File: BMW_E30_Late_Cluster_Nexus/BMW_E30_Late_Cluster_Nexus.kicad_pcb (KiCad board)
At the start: 2 copper layers, 356.8 x 150 mm, 19 parts, among them J1 Blue, J2 White, J3 Yellow

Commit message: All Footprints Added to Nexus
All footprints have been added to the nexus board project. Next step is to import them to the layout.
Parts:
- moved J1 1.00 mm to (337.1, 162.8)
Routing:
- net Brake lining: track 594.6 -> 0.00 mm
- net 12V: track 522.6 -> 0.00 mm
- net GND: track 411.4 -> 0.00 mm
- net GND lighting: track 365.4 -> 0.00 mm
- net Park brake: track 240.4 -> 0.00 mm
- net Turn L: track 176.8 -> 0.00 mm
- net High beam: track 157.1 -> 0.00 mm
- net Turn R: track 156.1 -> 0.00 mm
- net Check: track 135.2 -> 0.00 mm
- net Brake fluid: track 115.9 -> 0.00 mm
- net Fog front: track 95.5 -> 0.00 mm
- net Fog rear: track 57.6 -> 0.00 mm
- net Oil pressure: track 57.0 -> 0.00 mm
- net Temp warn: track 50.0 -> 0.00 mm
- net Fuel warn: track 33.9 -> 0.00 mm

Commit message: Nexus Layout Updates
Layout is about 50% complete. Need to verify exact component locations with early model board.
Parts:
- added D6: 1N4004, Diode_THT:D_DO-41_SOD81_P12.70mm_Horizontal, B.Cu at (332.1, 228.0)
- added D64: 1N4004, Diode_THT:D_DO-41_SOD81_P10.16mm_Horizontal, B.Cu at (220.1, 126.9)
- added D7: 1N4004, Diode_THT:D_DO-41_SOD81_P12.70mm_Horizontal, B.Cu at (53.6, 154.8)
- added D8: 1N4004, Diode_THT:D_DO-41_SOD81_P12.70mm_Horizontal, B.Cu at (303.6, 162.8)
- added J4: Speedometer, BMW_Cluster_Connectors:ConnectorIV_Late, F.Cu at (213.9, 130.7)
- added J5: SI Connector, BMW_Cluster_Connectors:ConnectorV_Late, F.Cu at (240.1, 221.2)
- added J6: Tachometer, BMW_Cluster_Connectors:Tach_EG_Socket_Late, F.Cu at (227.1, 150.5)
- added Q1: BC327, Package_TO_SOT_THT:TO-92_Inline_Wide, B.Cu at (60.6, 148.0)
- added R10: 10k, Resistor_THT:R_Axial_DIN0207_L6.3mm_D2.5mm_P10.16mm_Horizontal, B.Cu at (314.1, 172.5)
- added R100: ??, Resistor_THT:R_Axial_DIN0207_L6.3mm_D2.5mm_P15.24mm_Horizontal, B.Cu at (61.1, 153.8)
- added R101: ??, Resistor_THT:R_Axial_DIN0207_L6.3mm_D2.5mm_P15.24mm_Horizontal, B.Cu at (57.6, 153.8)
- added R11: 4k7, Resistor_THT:R_Axial_DIN0207_L6.3mm_D2.5mm_P15.24mm_Horizontal, B.Cu at (67.6, 168.2)
- added R12: 390R 0W5, Resistor_THT:R_Axial_DIN0309_L9.0mm_D3.2mm_P15.24mm_Horizontal, B.Cu at (68.6, 149.5)
- added R2: 150R, Resistor_THT:R_Axial_DIN0414_L11.9mm_D4.5mm_P20.32mm_Horizontal, B.Cu at (338.6, 186.7)
- added R3: 68R 1W, Resistor_THT:R_Axial_DIN0414_L11.9mm_D4.5mm_P20.32mm_Horizontal, B.Cu at (53.6, 176.2)
- added R5: 220R 1W, Resistor_THT:R_Axial_DIN0414_L11.9mm_D4.5mm_P20.32mm_Horizontal, B.Cu at (377.8, 162.0)
- added R9: 10R, Resistor_THT:R_Axial_DIN0207_L6.3mm_D2.5mm_P15.24mm_Horizontal, B.Cu at (300.6, 190.8)
- added U1: Coolant Temp, BMW_Cluster_Connectors:Gauge_Temp, F.Cu at (354.3, 186.5)
- added U2: Fuel Gauge, BMW_Cluster_Connectors:Gauge_Fuel, F.Cu at (62.9, 186.5)
- J1: footprint TE_AMP:TE_827881-3 -> BMW_Cluster_Connectors:TE_827881-3
- J2: footprint TE_AMP:TE_827881-2 -> BMW_Cluster_Connectors:TE_827881-2
- J3: footprint TE_AMP:TE_827881-1 -> BMW_Cluster_Connectors:TE_827881-1
- LA1, LA2: footprint mount:2821MF -> BMW_Cluster_Connectors:2821MF
- LA10: value Brake lining -> Brake pad; footprint mount:2721MF -> BMW_Cluster_Connectors:2721MF
- LA11, LA12, LA15, LA16, LA3, LA4, LA5, LA6, LA9: footprint mount:2721MF -> BMW_Cluster_Connectors:2721MF
- LA13: value Oil pressure -> Oil Pressure; footprint mount:2721MF -> BMW_Cluster_Connectors:2721MF
- LA14: value Fuel reserve -> Fuel Reserve; footprint mount:2721MF -> BMW_Cluster_Connectors:2721MF
- LA7: value Fog rear -> Fog Rear; footprint mount:2721MF -> BMW_Cluster_Connectors:2721MF
- LA8: value Fog front -> Fog Front; footprint mount:2721MF -> BMW_Cluster_Connectors:2721MF
- moved LA7 19.9 mm to (147.5, 212.2), turned to 0 degrees
- moved LA8 19.9 mm to (127.6, 212.2), turned to 90 degrees
- turned LA1 to 0 degrees
- turned LA2 to -40 degrees
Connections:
- net 5V renamed S-DKV
- net Fog front renamed Fog_ind+
- net High beam renamed High_beam_ind
- net R renamed +12_T15_ACC
- net Turn L renamed LH_ind
- net Turn R renamed RH_ind
- J1 pad 1: 12V -> +12_Start_T50
- J1 pad 10: unconnected-(J1-Pin_10-Pad10) -> +12_T15
- J1 pad 11: unconnected-(J1-Pin_11-Pad11) -> Fuel_rate_input
- J1 pad 14: Battery 1 -> Charge_ind+
- J1 pad 16: Battery 2 -> Charge_ind-
- J1 pad 17: Brake fluid -> Brake_fluid_ind-
- J1 pad 18: Oil pressure -> OIl_pressure_ind-
- J1 pad 19: unconnected-(J1-Pin_19-Pad19) -> +12_T15
- J1 pad 2: 12V -> +12_T30
- J1 pad 20: GND -> GNDPWR
- J1 pad 21: Brake lining -> Brake_wear_sig_1
- J1 pad 22: SI reset -> SI_RST
- J1 pad 23: 12V -> +12_T15
- J1 pad 25: Temp warn -> Overheat_ind-
- J1 pad 26: Temp gauge -> Eng_temp_sensor
- J1 pad 3: unconnected-(J1-Pin_3-Pad3) -> Charge_ind-
- J1 pad 6: unconnected-(J1-Pin_6-Pad6) -> +12_T15
- J1 pad 7: 12V -> Raw_RPM_input
- J1 pad 8: unconnected-(J1-Pin_8-Pad8) -> Reverse_gear
- J1 pad 9: unconnected-(J1-Pin_9-Pad9) -> 5th_gear
- J2 pad 1: Park brake -> Park_brake_ind-
- J2 pad 10: unconnected-(J2-Pin_10-Pad10) -> Wheel_spd_output
- J2 pad 12: unconnected-(J2-Pin_12-Pad12) -> Wheel_spd_input
- J2 pad 14: Fog rear -> Rear_fog_ind+
- J2 pad 15: unconnected-(J2-Pin_15-Pad15) -> DKV-DEFEKT
- J2 pad 16: GND -> GNDPWR
- J2 pad 19: unconnected-(J2-Pin_19-Pad19) -> KL_31h
- J2 pad 2: unconnected-(J2-Pin_2-Pad2) -> N-DKV
- J2 pad 21: GND -> GNDPWR
- J2 pad 23: 12V -> Illum+
- J2 pad 24: GND lighting -> Illum-
- J2 pad 26: Brake lining -> Brake_wear_sig_2
- J2 pad 3: GND -> GNDPWR
- J2 pad 4: Fuel gauge -> Fuel_level
- J2 pad 5: Fuel warn -> Low_Fuel_ind-
- J2 pad 6: 12V -> +12_T15
- J2 pad 8: GND -> GNDPWR
- J2 pad 9: unconnected-(J2-Pin_9-Pad9) -> K-DKV
- J3 pad 1: GND -> GNDPWR
- J3 pad 10: 12V -> +12_T30
- J3 pad 11: 12V -> Engine_spd_input
- J3 pad 12: unconnected-(J3-Pin_12-Pad12) -> Fuel_rate_input
- J3 pad 14: 12V -> +12_T15
- J3 pad 15: 12V -> +12_T15
- J3 pad 16: unconnected-(J3-Pin_16-Pad16) -> GNDPWR
- J3 pad 17: unconnected-(J3-Pin_17-Pad17) -> Low_Fuel_ind-
- J3 pad 18: unconnected-(J3-Pin_18-Pad18) -> Fuel_level
- J3 pad 19: Park brake -> GNDPWR
- J3 pad 2: 12V -> +12_T15
- J3 pad 20: 12V -> Illum+
- J3 pad 21: GND lighting -> Illum-
- J3 pad 22: 12V -> +12_Start_T50
- J3 pad 23: 12V -> +12_T30
- J3 pad 24: 12V -> Engine_spd_input
- J3 pad 25: unconnected-(J3-Pin_25-Pad25) -> Fuel_rate_input
- J3 pad 26: Analog speed -> Wheel_spd_output
- J3 pad 3: unconnected-(J3-Pin_3-Pad3) -> GNDPWR
- J3 pad 4: Fuel warn -> Low_Fuel_ind-
- J3 pad 5: Fuel gauge -> Fuel_level
- J3 pad 6: Park brake -> GNDPWR
- J3 pad 7: 12V -> Illum+
- J3 pad 8: GND lighting -> Illum-
- J3 pad 9: 12V -> +12_Start_T50
- LA1 pad 1: 12V -> Illum-
- LA1 pad 2: GND lighting -> Illum+
- LA10 pad 1: 12V -> GNDPWR
- LA10 pad 2: Brake lining -> Net-(LA10-+)
- LA11 pad 1: 12V -> Brake_fluid_ind-
- LA11 pad 2: Brake fluid -> +12_T15
- LA12 pad 1: unconnected-(LA12---Pad1) -> Charge_ind+
- LA12 pad 2: unconnected-(LA12-+-Pad2) -> Charge_ind-
- LA13 pad 1: 12V -> OIl_pressure_ind-
- LA13 pad 2: Oil pressure -> +12_T15
- LA14 pad 1: 12V -> +12_T15
- LA14 pad 2: Fuel warn -> Low_Fuel_ind-
- LA15 pad 1: Temp warn -> +12_T15
- LA15 pad 2: 12V -> Overheat_ind-
- LA2 pad 1: 12V -> Illum+
- LA2 pad 2: GND lighting -> Illum-
- LA3 pad 1: GND -> +12_T15
- LA4 pad 2: GND -> GNDPWR
- LA5 pad 2: GND -> GNDPWR
- LA6 pad 1: GND -> GNDPWR
- LA7 pad 1: Fog rear -> GNDPWR
- LA7 pad 2: GND -> Rear_fog_ind+
- LA8 pad 2: GND -> GNDPWR
- LA9 pad 1: 12V -> +12_T15
- LA9 pad 2: Park brake -> Park_brake_ind-
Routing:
- net GNDPWR: track 0.00 -> 764.2 mm, vias 0 -> 2
- net +12_T15: track 0.00 -> 497.3 mm, vias 0 -> 2
- net Illum+: track 0.00 -> 457.5 mm, vias 0 -> 2
- net Illum-: track 0.00 -> 420.2 mm, vias 0 -> 2
- net Wheel_spd_output: track 0.00 -> 369.4 mm
- net Park_brake_ind-: track 0.00 -> 364.9 mm, vias 0 -> 4
- net +12_T15_ACC: track 0.00 -> 359.9 mm, vias 0 -> 2
- net Low_Fuel_ind-: track 0.00 -> 298.7 mm
- net Fuel_level: track 0.00 -> 281.2 mm
- net Wheel_spd_input: track 0.00 -> 259.2 mm
- net Net-(D8-K): track 0.00 -> 238.2 mm, vias 0 -> 2
- net LH_ind: track 0.00 -> 232.8 mm
- net +12_T30: track 0.00 -> 220.5 mm, vias 0 -> 2
- net Fuel_rate_input: track 0.00 -> 200.0 mm
- net Check: track 0.00 -> 168.6 mm, vias 0 -> 2
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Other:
- outline, holes or cut-outs redrawn
- board text added: "BMW PN: 1 377 374 or 1 381 952"
- board text added: "E30"
- board text added: "Glow Plug [Diesel]"
- board text added: "Nexus board replacement"
- board text added: "Revision: 1"
- board text removed: "1 377 374"
- board text removed: "E 30"
- board text removed: "Glow plug [Diesel]"
- board text removed: "Main board replacement"
- board text removed: "Polytechnic"
- board text removed: "Systems"

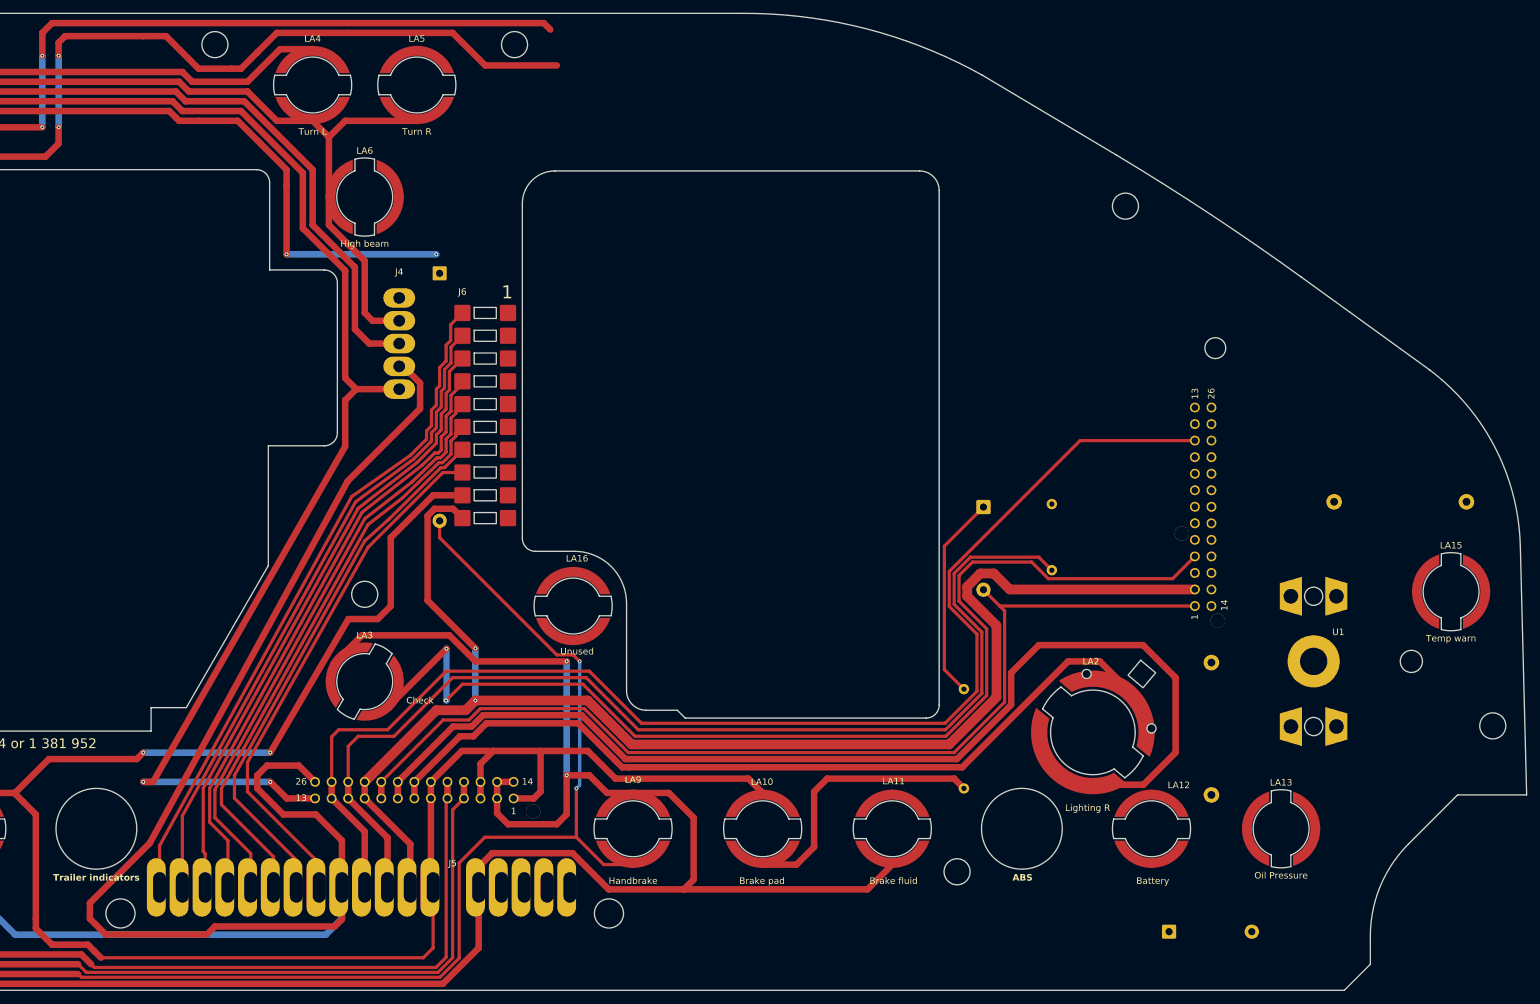
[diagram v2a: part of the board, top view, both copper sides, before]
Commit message: Nexus Trace Layout Completed
Trace layout is complete. Still need to verify some component locations
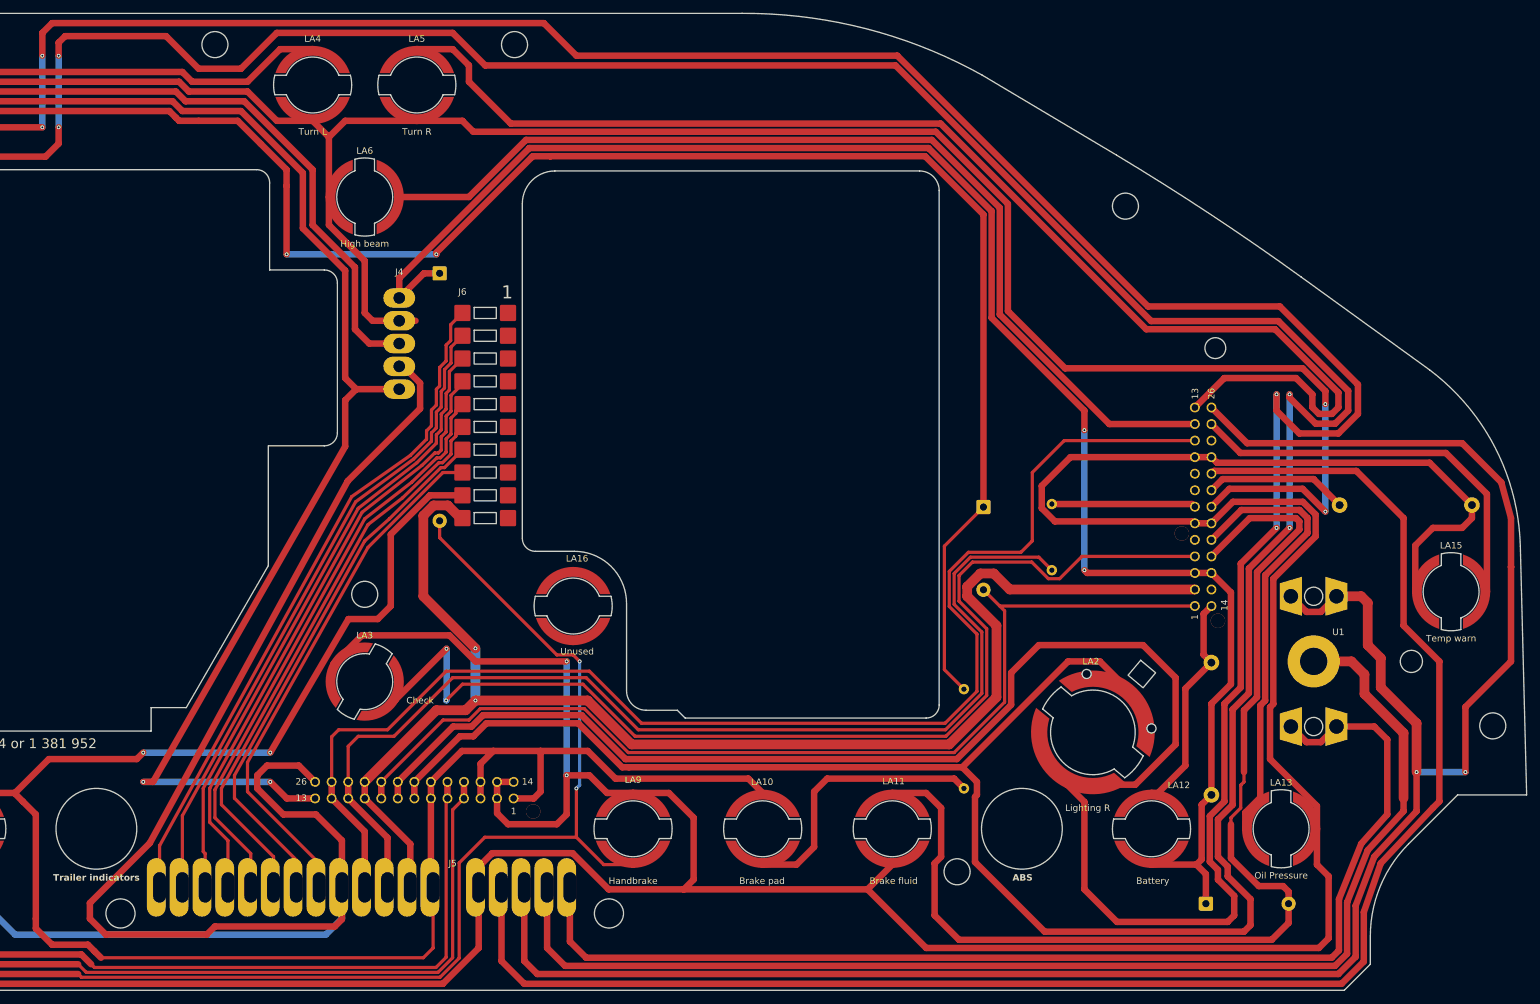
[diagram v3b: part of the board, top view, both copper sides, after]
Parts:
- moved D6 7.10 mm to (337.8, 223.7)
- moved R5 0.98 mm to (378.6, 162.5)
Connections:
- LA14 pad 1: +12_T15 -> unconnected-(LA14---Pad1)
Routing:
- net Eng_temp_sensor: track 0.00 -> 320.0 mm, vias 0 -> 2
- net Illum+: track 457.5 -> 765.6 mm, vias 2 -> 4
- net Illum-: track 420.2 -> 718.8 mm, vias 2 -> 4
- net +12_T15: track 497.3 -> 783.2 mm
- net Charge_ind-: track 0.00 -> 256.5 mm, vias 0 -> 2
- net SI_RST: track 0.00 -> 253.6 mm
- net GNDPWR: track 764.2 -> 971.9 mm, vias 2 -> 4
- net RH_ind: track 0.00 -> 194.9 mm
- net Temp_GND: track 0.00 -> 190.8 mm
- net Temp_+Ub: track 0.00 -> 180.1 mm
- net Brake_fluid_ind-: track 0.00 -> 170.3 mm
- net High_beam_ind: track 0.00 -> 153.3 mm
- net Net-(D8-K): track 238.2 -> 377.2 mm
- net OIl_pressure_ind-: track 0.00 -> 68.8 mm
- net Overheat_ind-: track 0.00 -> 61.7 mm
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
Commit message: Rotate Right Illum Bulb
Changed orientation of the right side illumination bulb
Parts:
- turned LA2 to -30 degrees
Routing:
- net Illum-: track 718.8 -> 715.9 mm
- net Illum+: track 765.6 -> 764.0 mm

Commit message: Standardized Board Location In Editor
Made the board location the same in both projects so component locations can be corrected from sample runs of the early boards.
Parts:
- moved D6 0.60 mm to (337.1, 223.7)
- moved D8 0.60 mm to (303.0, 162.8)
- moved J1 0.60 mm to (336.5, 162.8)
- moved LA11 0.60 mm to (289.0, 212.2)
- moved LA13 0.60 mm to (348.7, 212.2)
- moved LA9 0.60 mm to (249.2, 212.2)
- moved R10 0.60 mm to (313.5, 172.5)
- moved R2 0.60 mm to (338.0, 186.7)
- moved R5 0.60 mm to (378.0, 162.5)
- moved R9 0.60 mm to (300.0, 190.8)
- moved U1 0.60 mm to (353.7, 186.5)
- moved D7 0.60 mm to (53.0, 154.8)
- moved LA14 0.60 mm to (42.8, 174.4)
- moved Q1 0.60 mm to (60.0, 148.0)
- moved R100 0.60 mm to (60.5, 153.8)
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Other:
- outline, holes or cut-outs redrawn

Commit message: Layout Updates to Match Early
Changed a few light bulb component locations to match the correct locations on the early model boards.
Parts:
- moved LA15 0.81 mm to (374.6, 175.0)
- moved LA14 0.45 mm to (43.0, 174.0)
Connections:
- LA14 pad 1: unconnected-(LA14---Pad1) -> +12_T15
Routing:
- net Wheel_spd_output: track 369.4 -> 370.6 mm
- net +12_T15: track 783.2 -> 782.3 mm
- net Overheat_ind-: track 61.7 -> 60.9 mm
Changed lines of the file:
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@@
 	(net 60 "Net-(U2-Vcc)")
 	(net 61 "Net-(LA10-+)")
-	(net 62 "unconnected-(LA14---Pad1)")
 	(footprint "BMW_Cluster_Connectors:2721MF"
 		(layer "F.Cu")
@@
 	(footprint "BMW_Cluster_Connectors:2721MF"
 		(layer "F.Cu")
-		(at 374.8 175.8 90)
+		(at 374.65 175 90)
 		(property "Reference" "LA15"
 			(at 7.099836 0.003178 0)
@@
 	(footprint "BMW_Cluster_Connectors:2721MF"
 		(layer "F.Cu")
-		(at 42.8 174.4 90)
+		(at 43 174 90)
 		(property "Reference" "LA14"
 			(at 7.099836 0.003178 0)
@@
 			(size 1 1)
 			(layers "F.Cu" "F.Mask")
-			(net 62 "unconnected-(LA14---Pad1)")
+			(net 13 "+12_T15")
 			(pinfunction "-")
 			(pintype "passive")
@@
 	)
 	(segment
-		(start 378 164.5)
-		(end 376.5 166)
+		(start 372 166)
+		(end 369.15 168.85)
 		(width 1)
 		(layer "F.Cu")
@@
 	)
 	(segment
-		(start 51.5 216.5)
-		(end 54.5 224)
-		(width 1)
-		(layer "F.Cu")
-		(net 13)
-	)
-	(segment
 		(start 221 182.5)
 		(end 207.58686 182.5)
@@
 	)
 	(segment
-		(start 372 166)
-		(end 369.3 168.7)
+		(start 225.5 221.2)
+		(end 225.5 230.5)
 		(width 1)
 		(layer "F.Cu")
@@
 	)
 	(segment
+		(start 225.5 230.5)
+		(end 220.001 235.999)
+		(width 1)
+		(layer "F.Cu")
+		(net 13)
+	)
+	(segment
+		(start 37.5 174)
+		(end 37.5 169.5)
+		(width 1)
+		(layer "F.Cu")
+		(net 13)
+	)
+	(segment
 		(start 41 166)
 		(end 51.5 166)
@@
 	)
 	(segment
-		(start 76.33 165.3)
-		(end 79.46 165.3)
+		(start 54.5 224)
+		(end 51.5 216.5)
 		(width 1)
 		(layer "F.Cu")
@@
 	)
 	(segment
-		(start 37.3 169.7)
-		(end 41 166)
+		(start 76.33 165.3)
+		(end 79.46 165.3)
 		(width 1)
 		(layer "F.Cu")
@@
 	)
 	(segment
-		(start 369.3 168.7)
-		(end 369.3 175.8)
+		(start 258.5 220)
+		(end 257 221.5)
 		(width 1)
 		(layer "F.Cu")
@@
 	)
 	(segment
-		(start 258.5 220)
-		(end 257 221.5)
+		(start 55 232.5)
+		(end 54.5 224)
 		(width 1)
 		(layer "F.Cu")
@@
 	)
 	(segment
-		(start 228.32 209.82)
-		(end 228.32 207.54)
+		(start 378 162.5)
+		(end 378 164.5)
 		(width 1)
 		(layer "F.Cu")
@@
 	)
 	(segment
-		(start 347 201.5)
-		(end 347 193.538362)
+		(start 228.32 209.82)
+		(end 228.32 207.54)
 		(width 1)
 		(layer "F.Cu")
@@
 	)
 	(segment
-		(start 376.5 166)
-		(end 372 166)
+		(start 347 201.5)
+		(end 347 193.538362)
 		(width 1)
 		(layer "F.Cu")
@@
 	)
 	(segment
-		(start 220.001 235.999)
-		(end 225.5 230.5)
+		(start 53 167.5)
+		(end 55.5 167.5)
 		(width 1)
 		(layer "F.Cu")
@@
 	)
 	(segment
-		(start 53 167.5)
-		(end 55.5 167.5)
+		(start 294.2 230.5)
+		(end 354.5 230.5)
 		(width 1)
 		(layer "F.Cu")
@@
 	)
 	(segment
-		(start 294.2 230.5)
-		(end 354.5 230.5)
+		(start 369.15 168.85)
+		(end 369.15 175)
 		(width 1)
 		(layer "F.Cu")
@@
 	)
 	(segment
+		(start 37.5 169.5)
+		(end 41 166)
+		(width 1)
+		(layer "F.Cu")
+		(net 13)
+	)
+	(segment
 		(start 378 162.5)
 		(end 371.5 156)
@@
 	)
 	(segment
-		(start 354.2 217.7)
-		(end 354.2 212.2)
+		(start 376.5 166)
+		(end 372 166)
 		(width 1)
 		(layer "F.Cu")
@@
 	)
 	(segment
-		(start 38 203)
-		(end 51.5 216.5)
+		(start 354.2 217.7)
+		(end 354.2 212.2)
 		(width 1)
 		(layer "F.Cu")
@@
 	)
 	(segment
+		(start 220.001 235.999)
+		(end 58.499 235.999)
+		(width 1)
+		(layer "F.Cu")
+		(net 13)
+	)
+	(segment
 		(start 354.2 208.7)
 		(end 347 201.5)
@@
 	)
 	(segment
+		(start 58.499 235.999)
+		(end 55 232.5)
+		(width 1)
+		(layer "F.Cu")
+		(net 13)
+	)
+	(segment
+		(start 51.5 216.5)
+		(end 38 203)
+		(width 1)
+		(layer "F.Cu")
+		(net 13)
+	)
+	(segment
 		(start 352.036362 161.998)
 		(end 341.302 161.998)
@@
 	)
 	(segment
-		(start 38 195.355945)
-		(end 38 203)
+		(start 38 203)
+		(end 38 195)
 		(width 1)
 		(layer "F.Cu")
@@
 	)
 	(segment
-		(start 37.3 174.4)
-		(end 37.3 194.655945)
-		(width 1)
-		(layer "F.Cu")
-		(net 13)
-	)
-	(segment
 		(start 249.2 206.7)
 		(end 254.7 206.7)
@@
 	)
 	(segment
-		(start 378 162.5)
-		(end 378 164.5)
+		(start 378 164.5)
+		(end 376.5 166)
 		(width 1)
 		(layer "F.Cu")
@@
 	)
 	(segment
-		(start 58.499 235.999)
-		(end 220.001 235.999)
-		(width 1)
-		(layer "F.Cu")
-		(net 13)
-	)
-	(segment
 		(start 354.5 230.5)
 		(end 356 229)
@@
 	)
 	(segment
-		(start 37.3 174.4)
-		(end 37.3 169.7)
+		(start 37.5 194.5)
+		(end 37.5 174)
 		(width 1)
 		(layer "F.Cu")
@@
 	)
 	(segment
-		(start 54.5 224)
-		(end 55 232.5)
+		(start 38 195)
+		(end 37.5 194.5)
 		(width 1)
 		(layer "F.Cu")
@@
 	)
 	(segment
-		(start 37.3 194.655945)
-		(end 38 195.355945)
-		(width 1)
-		(layer "F.Cu")
-		(net 13)
-	)
-	(segment
 		(start 230 211.5)
 		(end 228.32 209.82)
@@
 		(net 13)
 	)
-	(segment
-		(start 55 232.5)
-		(end 58.499 235.999)
-		(width 1)
-		(layer "F.Cu")
-		(net 13)
-	)
-	(segment
-		(start 225.5 230.5)
-		(end 225.5 221.2)
-		(width 1)
-		(layer "F.Cu")
-		(net 13)
-	)
 	(via
 		(at 239 204)
@@
 	)
 	(segment
-		(start 380.3 160.8)
-		(end 374 154.5)
+		(start 374 154.5)
+		(end 380.15 160.65)
 		(width 1)
 		(layer "F.Cu")
@@
 	)
 	(segment
-		(start 380.3 175.8)
-		(end 380.3 160.8)
+		(start 380.15 160.65)
+		(end 380.15 175)
 		(width 1)
 		(layer "F.Cu")
@@
 	)
 	(segment
-		(start 108.873357 183)
-		(end 78.5 183)
+		(start 204.5 221.2)
+		(end 204.5 226)
 		(width 1)
 		(layer "B.Cu")
@@
 	)
 	(segment
-		(start 204.5 226)
-		(end 202.062933 228.437067)
+		(start 154.310424 228.437067)
+		(end 108.873357 183)
 		(width 1)
 		(layer "B.Cu")
@@
 	)
 	(segment
-		(start 204.5 221.2)
-		(end 204.5 226)
+		(start 73.5 180)
+		(end 73.5 157.5)
 		(width 1)
 		(layer "B.Cu")
@@
 	)
 	(segment
-		(start 73.5 178)
-		(end 73.5 157.5)
+		(start 108.873357 183)
+		(end 76.5 183)
 		(width 1)
 		(layer "B.Cu")
@@
 	)
 	(segment
-		(start 154.310424 228.437067)
-		(end 108.873357 183)
+		(start 73.5 157.5)
+		(end 75.86 155.14)
 		(width 1)
 		(layer "B.Cu")
@@
 	)
 	(segment
-		(start 75.86 155.14)
-		(end 79.46 155.14)
+		(start 204.5 226)
+		(end 202.062933 228.437067)
 		(width 1)
 		(layer "B.Cu")
@@
 	)
 	(segment
-		(start 202.062933 228.437067)
-		(end 154.310424 228.437067)
+		(start 76.5 183)
+		(end 73.5 180)
 		(width 1)
 		(layer "B.Cu")
@@
 	)
 	(segment
-		(start 73.5 157.5)
-		(end 75.86 155.14)
+		(start 202.062933 228.437067)
+		(end 154.310424 228.437067)
 		(width 1)
 		(layer "B.Cu")
@@
 	)
 	(segment
-		(start 78.5 183)
-		(end 73.5 178)
+		(start 75.86 155.14)
+		(end 79.46 155.14)
 		(width 1)
 		(layer "B.Cu")
